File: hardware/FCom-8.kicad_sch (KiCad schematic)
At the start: 29 parts, among them J101 Conn_01x04, SW101 SW_DIP_x08, SW102 SW_DIP_x08, SW104 SW_DIP_x04, SW105 G19AP, U101 W65C02S6TPG-14, U102 AS6C1008-55PCN, U103 W65C22N6TPG-14, U104 74LS04, U105 74LS08, U106 74LS21, Y101 ECS-100AX-010

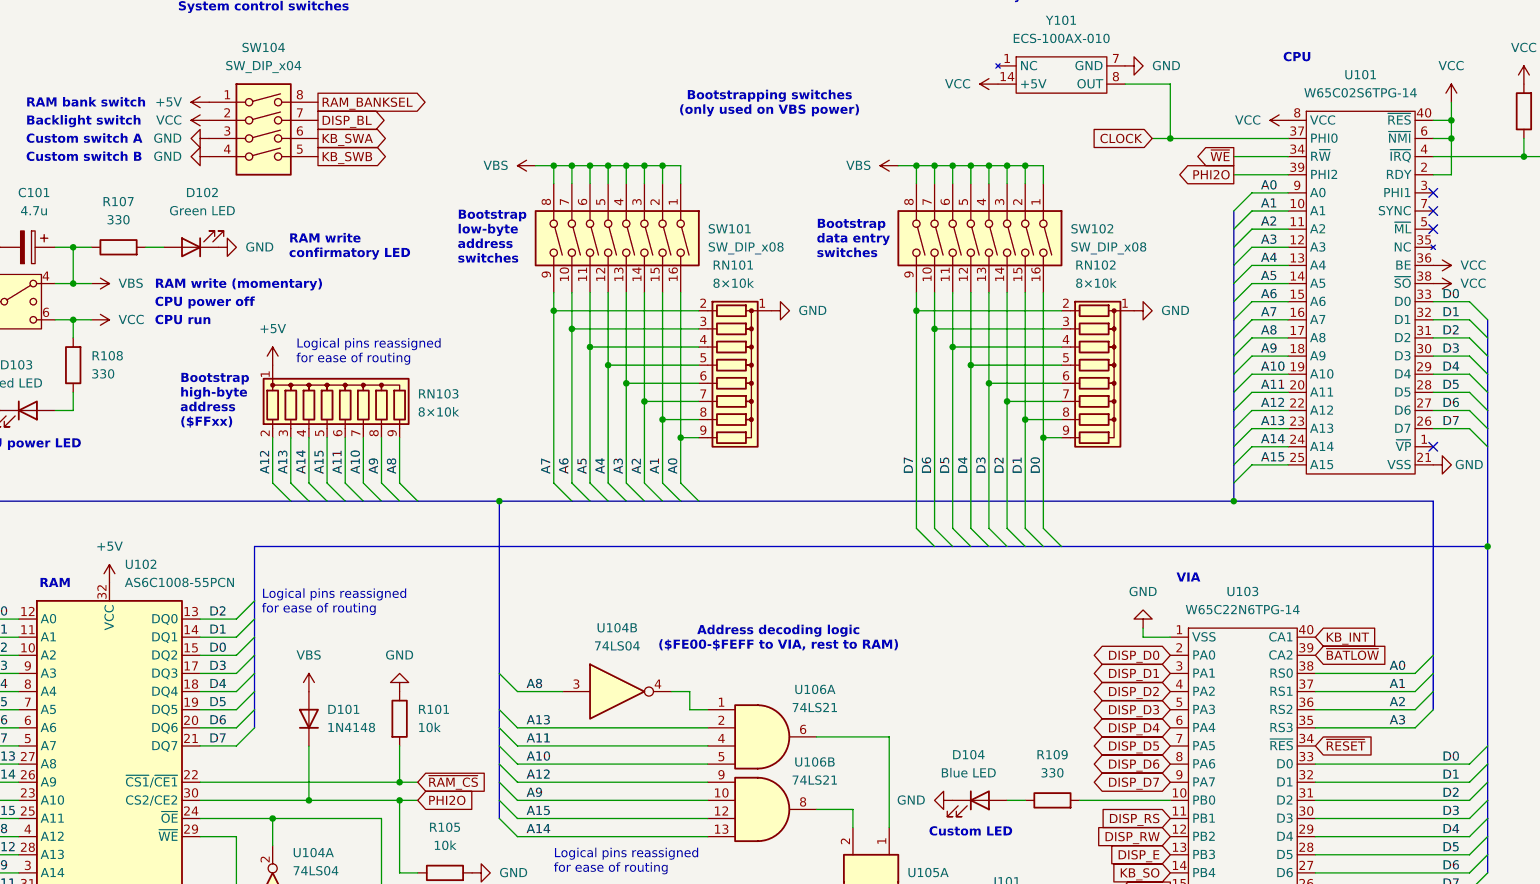
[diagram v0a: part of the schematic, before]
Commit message: Finish rough component wiring layout
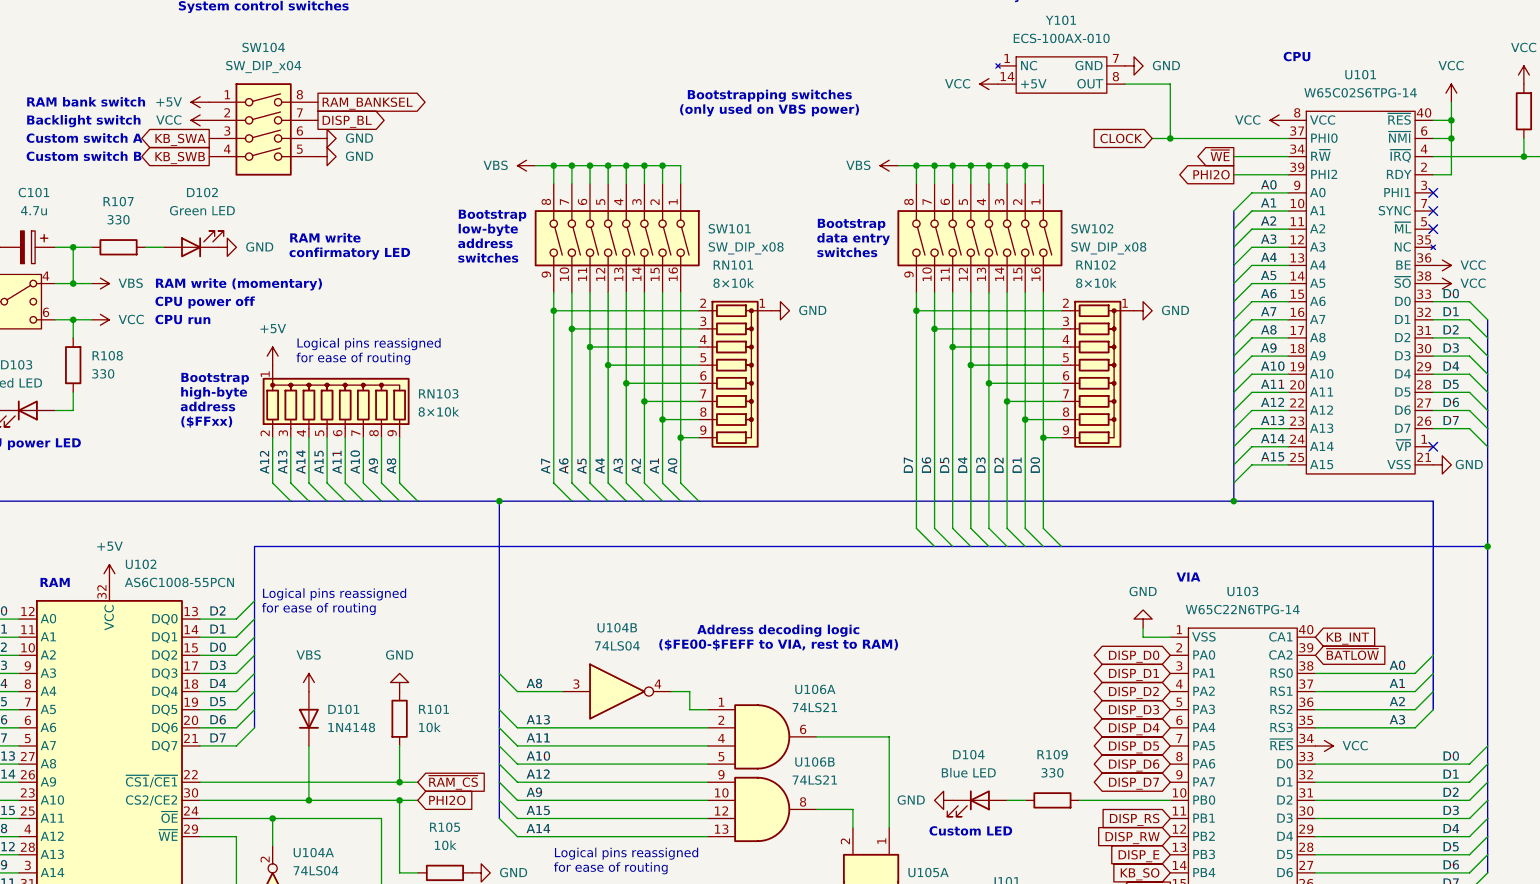
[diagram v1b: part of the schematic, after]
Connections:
- net ~{RESET} is gone; now on net VCC: U103.34 (~{RES})
- net GND: now also SW104.5, SW104.6; no longer SW104.3, SW104.4
- net KB_SWA: now also SW104.3; no longer SW104.6
- net KB_SWB: now also SW104.4; no longer SW104.5
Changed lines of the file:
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@@
 		)
 	)
-	(global_label "KB_SWB"
-		(shape output)
-		(at 95.25 39.37 0)
-		(fields_autoplaced yes)
-		(effects
-			(font
-				(size 1.27 1.27)
-			)
-			(justify left)
-		)
-		(property "Intersheetrefs" "${INTERSHEET_REFS}"
-			(at 105.6737 39.37 0)
-			(effects
-				(font
-					(size 1.27 1.27)
-				)
-				(justify left)
-				(hide yes)
-			)
-		)
-	)
 	(global_label "CLOCK"
 		(shape input)
@@
 		)
 	)
-	(global_label "KB_SWA"
+	(global_label "KB_SWB"
 		(shape output)
-		(at 95.25 36.83 0)
+		(at 80.01 39.37 180)
 		(fields_autoplaced yes)
 		(effects
@@
 				(size 1.27 1.27)
 			)
-			(justify left)
+			(justify right)
 		)
 		(property "Intersheetrefs" "${INTERSHEET_REFS}"
-			(at 105.4923 36.83 0)
+			(at 69.5863 39.37 0)
 			(effects
 				(font
 					(size 1.27 1.27)
 				)
-				(justify left)
+				(justify right)
 				(hide yes)
 			)
@@
 		)
 	)
-	(global_label "~{RESET}"
-		(shape input)
-		(at 234.95 121.92 0)
+	(global_label "KB_SCK"
+		(shape output)
+		(at 214.63 144.78 180)
 		(fields_autoplaced yes)
 		(effects
@@
 				(size 1.27 1.27)
 			)
-			(justify left)
+			(justify right)
 		)
 		(property "Intersheetrefs" "${INTERSHEET_REFS}"
-			(at 243.6803 121.92 0)
+			(at 204.3877 144.78 0)
 			(effects
 				(font
 					(size 1.27 1.27)
 				)
-				(justify left)
+				(justify right)
 				(hide yes)
 			)
 		)
 	)
-	(global_label "KB_SCK"
-		(shape output)
-		(at 214.63 144.78 180)
+	(global_label "CLOCK"
+		(shape input)
+		(at 212.09 36.83 180)
 		(fields_autoplaced yes)
 		(effects
@@
 		)
 		(property "Intersheetrefs" "${INTERSHEET_REFS}"
-			(at 204.3877 144.78 0)
+			(at 202.9362 36.83 0)
 			(effects
 				(font
@@
 		)
 	)
-	(global_label "CLOCK"
+	(global_label "~{WE}"
 		(shape input)
-		(at 212.09 36.83 180)
+		(at 83.82 157.48 270)
 		(fields_autoplaced yes)
 		(effects
@@
 		)
 		(property "Intersheetrefs" "${INTERSHEET_REFS}"
-			(at 202.9362 36.83 0)
+			(at 83.82 163.0656 90)
 			(effects
 				(font
@@
 		)
 	)
-	(global_label "~{WE}"
-		(shape input)
-		(at 83.82 157.48 270)
+	(global_label "KB_SWA"
+		(shape output)
+		(at 80.01 36.83 180)
 		(fields_autoplaced yes)
 		(effects
@@
 		)
 		(property "Intersheetrefs" "${INTERSHEET_REFS}"
-			(at 83.82 163.0656 90)
+			(at 69.7677 36.83 0)
 			(effects
 				(font
@@
 	(symbol
 		(lib_id "power:GND")
-		(at 80.01 39.37 270)
+		(at 95.25 39.37 90)
+		(mirror x)
 		(unit 1)
 		(exclude_from_sim no)
@@
 		(fields_autoplaced yes)
 		(property "Reference" "#PWR0139"
-			(at 73.66 39.37 0)
+			(at 101.6 39.37 0)
 			(effects
 				(font
@@
 		)
 		(property "Value" "GND"
-			(at 76.2 39.3699 90)
+			(at 99.06 39.3699 90)
 			(effects
 				(font
@@
 		)
 		(property "Footprint" ""
-			(at 80.01 39.37 0)
+			(at 95.25 39.37 0)
 			(effects
 				(font
@@
 		)
 		(property "Datasheet" ""
-			(at 80.01 39.37 0)
+			(at 95.25 39.37 0)
 			(effects
 				(font
@@
 		)
 		(property "Description" "Power symbol creates a global label with name \"GND\" , ground"
-			(at 80.01 39.37 0)
+			(at 95.25 39.37 0)
 			(effects
 				(font
@@
 		)
 		(instances
-			(project ""
+			(project "FCom-8"
 				(path "/d870bcaf-2f1b-46ce-b0b4-300d405a54b8"
 					(reference "#PWR0139")
@@
 	(symbol
 		(lib_id "power:GND")
-		(at 80.01 36.83 270)
+		(at 95.25 36.83 90)
+		(mirror x)
 		(unit 1)
 		(exclude_from_sim no)
@@
 		(fields_autoplaced yes)
 		(property "Reference" "#PWR0138"
-			(at 73.66 36.83 0)
+			(at 101.6 36.83 0)
 			(effects
 				(font
@@
 		)
 		(property "Value" "GND"
-			(at 76.2 36.8299 90)
+			(at 99.06 36.8299 90)
 			(effects
 				(font
@@
 		)
 		(property "Footprint" ""
-			(at 80.01 36.83 0)
+			(at 95.25 36.83 0)
 			(effects
 				(font
@@
 		)
 		(property "Datasheet" ""
-			(at 80.01 36.83 0)
+			(at 95.25 36.83 0)
 			(effects
 				(font
@@
 		)
 		(property "Description" "Power symbol creates a global label with name \"GND\" , ground"
-			(at 80.01 36.83 0)
+			(at 95.25 36.83 0)
 			(effects
 				(font
@@
 		)
 		(instances
-			(project ""
+			(project "FCom-8"
 				(path "/d870bcaf-2f1b-46ce-b0b4-300d405a54b8"
 					(reference "#PWR0138")
@@
 					(unit 1)
 				)
+			)
+		)
+	)
+	(symbol
+		(lib_id "power:VCC")
+		(at 234.95 121.92 270)
+		(unit 1)
+		(exclude_from_sim no)
+		(in_bom yes)
+		(on_board yes)
+		(dnp no)
+		(fields_autoplaced yes)
+		(property "Reference" "#PWR0145"
+			(at 231.14 121.92 0)
+			(effects
+				(font
+					(size 1.27 1.27)
+				)
+				(hide yes)
+			)
+		)
+		(property "Value" "VCC"
+			(at 238.76 121.9199 90)
+			(effects
+				(font
+					(size 1.27 1.27)
+				)
+				(justify left)
+			)
+		)
+		(property "Footprint" ""
+			(at 234.95 121.92 0)
+			(effects
+				(font
+					(size 1.27 1.27)
+				)
+				(hide yes)
+			)
+		)
+		(property "Datasheet" ""
+			(at 234.95 121.92 0)
+			(effects
+				(font
+					(size 1.27 1.27)
+				)
+				(hide yes)
+			)
+		)
+		(property "Description" "Power symbol creates a global label with name \"VCC\""
+			(at 234.95 121.92 0)
+			(effects
+				(font
+					(size 1.27 1.27)
+				)
+				(hide yes)
+			)
+		)
+		(pin "1"
+		)
+		(instances
+			(project "FCom-8"
+				(path "/d870bcaf-2f1b-46ce-b0b4-300d405a54b8"
+					(reference "#PWR0145")
+					(unit 1)
+				)
